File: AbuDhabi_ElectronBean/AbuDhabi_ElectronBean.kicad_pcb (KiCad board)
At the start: 2 copper layers, 174.2 x 163.6 mm, 18 parts, among them J12 Sensor, J13 Bomba, J14 Eingang - obere Pins, J15 Eingang - obere Pins, J16 Power, J17 Control, J18 Data, J19 Ext. versorgung conn, J20 MUX_output, U1 74HC139P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

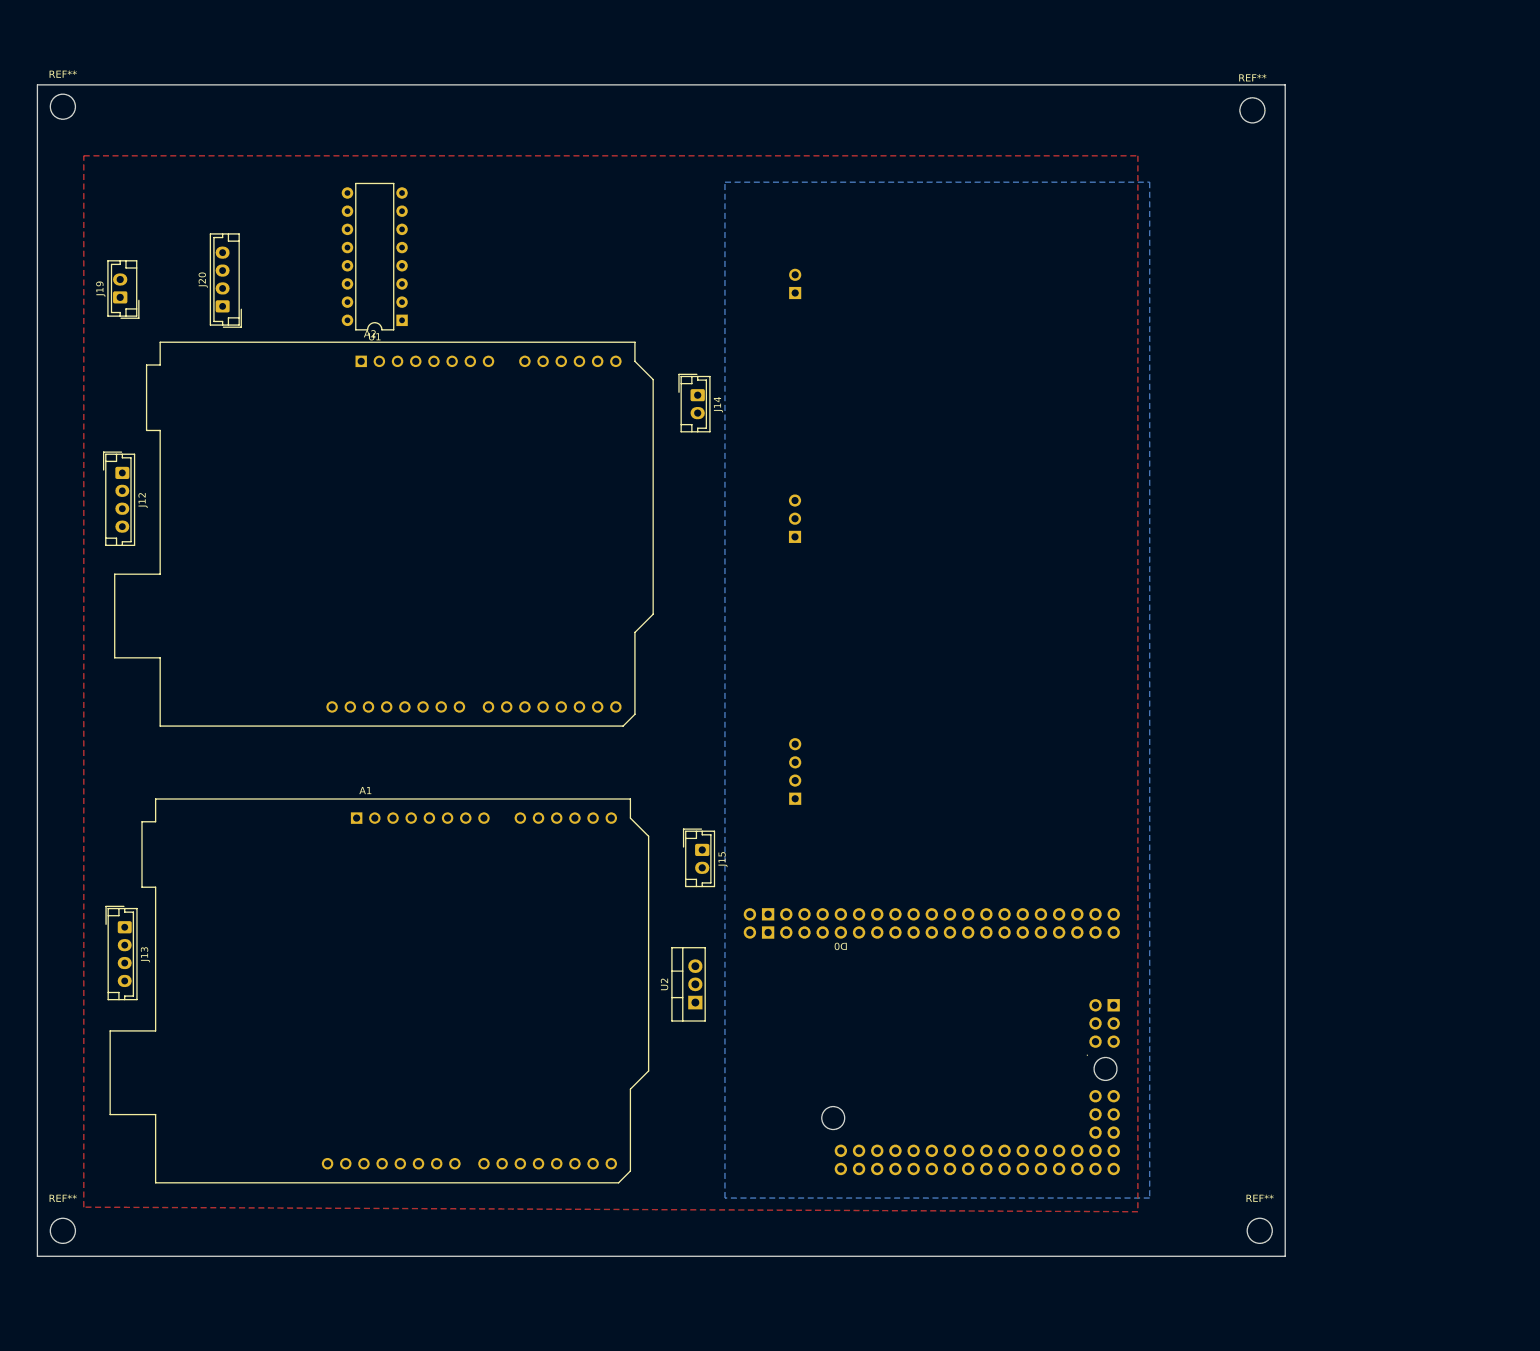
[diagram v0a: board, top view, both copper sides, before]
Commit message: Arduino Mega footpring change and LEDs addition
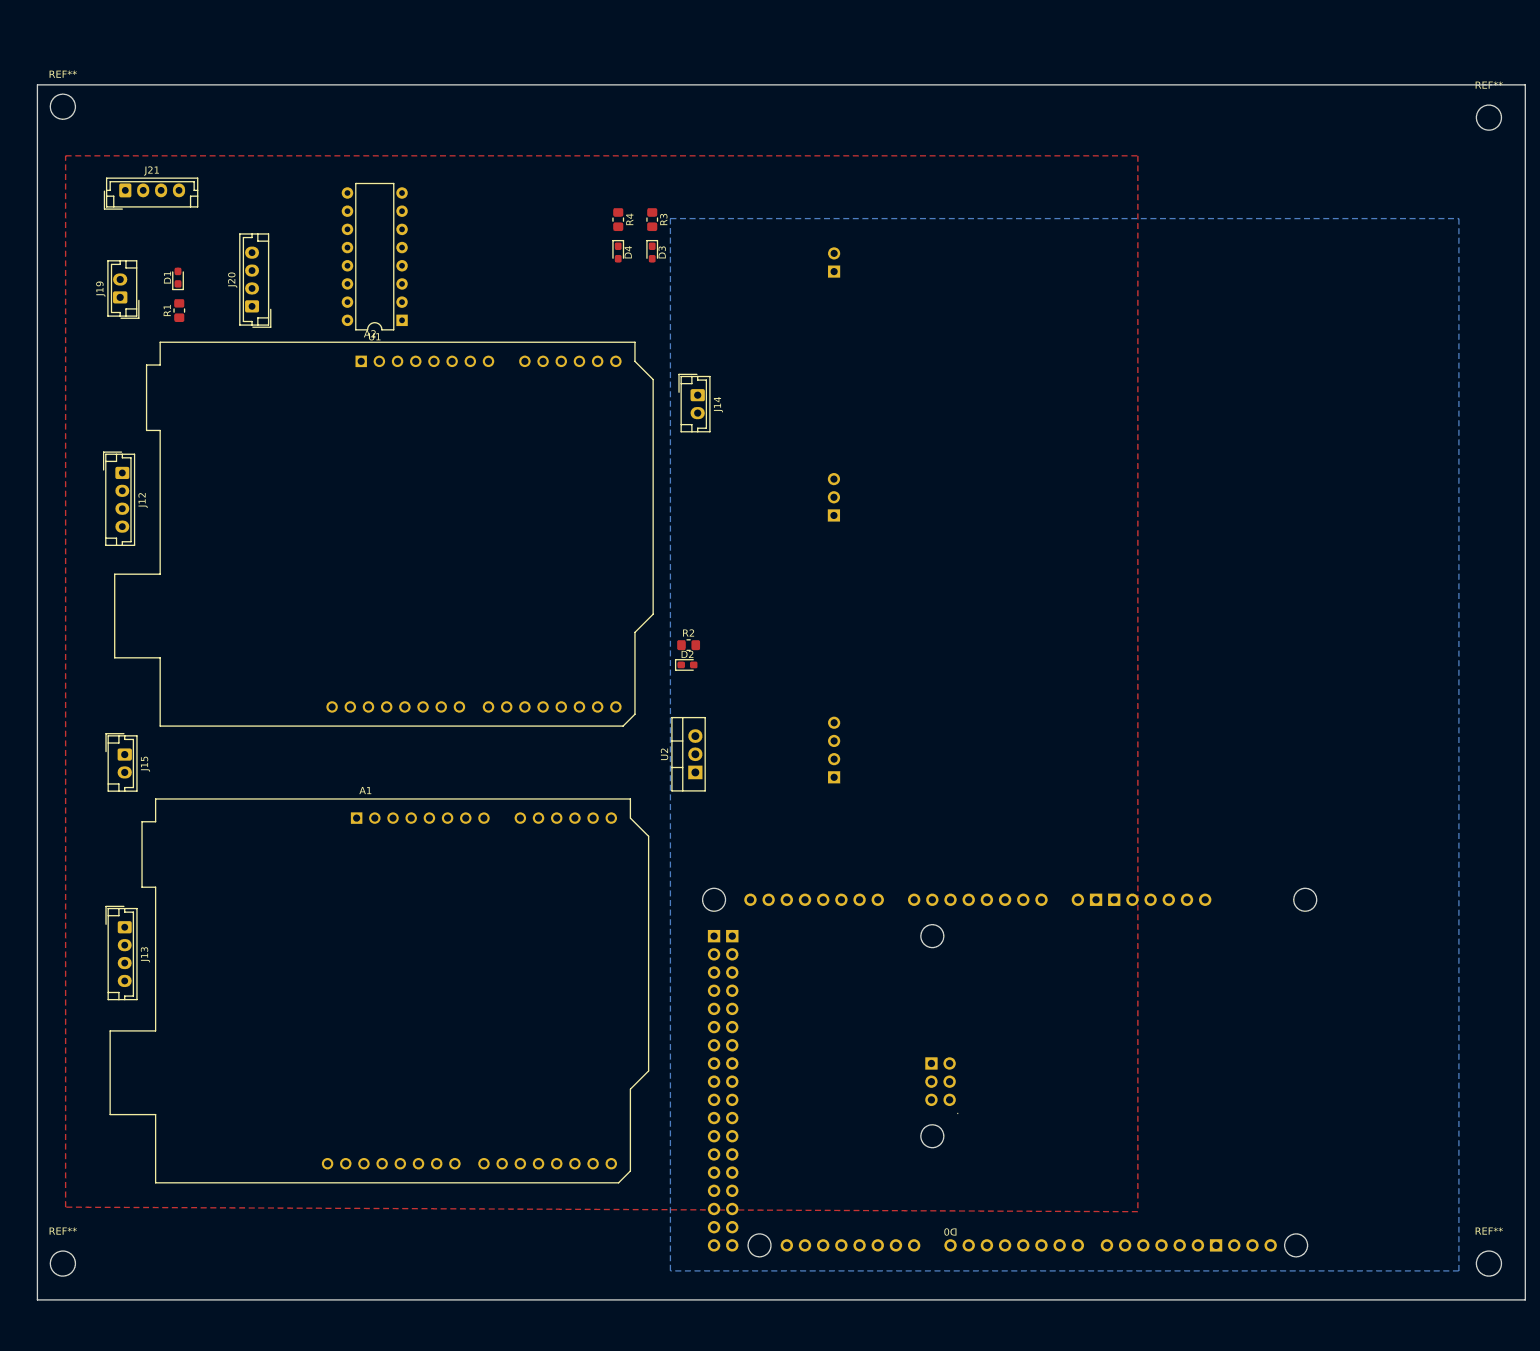
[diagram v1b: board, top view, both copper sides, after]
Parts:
- added D1: LED, LED_SMD:LED_0603_1608Metric_Pad1.05x0.95mm_HandSolder, F.Cu at (40.5, 47.7)
- added D2: LED, LED_SMD:LED_0603_1608Metric_Pad1.05x0.95mm_HandSolder, F.Cu at (111.6, 101.8)
- added D3: LED, LED_SMD:LED_0603_1608Metric_Pad1.05x0.95mm_HandSolder, F.Cu at (106.7, 44.2)
- added D4: LED, LED_SMD:LED_0603_1608Metric_Pad1.05x0.95mm_HandSolder, F.Cu at (101.9, 44.2)
- added J21: Versorgung(opt), Connector_JST:JST_EH_B4B-EH-A_1x04_P2.50mm_Vertical, F.Cu at (33.1, 35.6)
- added R1: 220, Resistor_SMD:R_0805_2012Metric_Pad1.20x1.40mm_HandSolder, F.Cu at (40.6, 52.3)
- added R2: 220, Resistor_SMD:R_0805_2012Metric_Pad1.20x1.40mm_HandSolder, F.Cu at (111.8, 99.1)
- added R3: 220, Resistor_SMD:R_0805_2012Metric_Pad1.20x1.40mm_HandSolder, F.Cu at (106.7, 39.6)
- added R4: 220, Resistor_SMD:R_0805_2012Metric_Pad1.20x1.40mm_HandSolder, F.Cu at (101.9, 39.6)
- A3: footprint Arduino:Footprint_Mega2560_Pro_Socket -> Arduino:Arduino_Mega2560_R3_Shield; moved to F.Cu
- moved A3 102.2 mm to (211.8, 132.1), turned to 180 degrees
- moved J15 81.7 mm to (33.0, 114.3)
- moved REF** 33.0 mm to (223.5, 25.4)
- moved REF** 32.3 mm to (223.5, 185.4)
- moved U2 32.1 mm to (112.7, 116.8)
- moved J16 6.20 mm to (132.1, 46.9)
- moved J17 6.20 mm to (132.1, 81.0)
- moved J18 6.20 mm to (132.1, 117.5)
- moved REF** 4.57 mm to (24.4, 185.4)
- moved J20 4.11 mm to (50.8, 51.8)
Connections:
- A2 pad 15: /Rx1 -> /Rx3
- A2 pad 16: /Tx1 -> /Tx3
- A3 pad D5: unconnected-(A3-PadD5) -> /IO5
- J12 pad 1: /GND ext -> GND
- J13 pad 1: /GND ext -> GND
- J16 pad 1: /GND Ard -> GND
- J16 pad 2: /5V -> /5VExt
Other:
- board size 174.2 x 163.6 mm -> 207.8 x 169.7 mm

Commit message: A bit of order
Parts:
- moved J20 2.54 mm to (53.3, 51.8)
- moved R1 2.30 mm to (41.6, 50.2)
- moved D1 2.30 mm to (41.4, 45.6)
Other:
- board text added: "24V ext. source"
- board text added: "5V first output"
- board text added: "Ard. output"
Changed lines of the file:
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@@
   )
   (footprint "LED_SMD:LED_0603_1608Metric_Pad1.05x0.95mm_HandSolder" (layer "F.Cu")
-    (at 40.46 47.745 90)
+    (at 41.375 45.63 90)
     (descr "LED SMD 0603 (1608 Metric), square (rectangular) end terminal, IPC_7351 nominal, (Body size source: http://www.tortai-tech.com/upload/download/2011102023233369053.pdf), generated with kicad-footprint-generator")
     (tags "LED handsolder")
@@
   )
   (footprint "Connector_JST:JST_EH_B4B-EH-A_1x04_P2.50mm_Vertical" (layer "F.Cu")
-    (at 50.8 51.756 90)
+    (at 53.34 51.756 90)
     (descr "JST EH series connector, B4B-EH-A (http://www.jst-mfg.com/product/pdf/eng/eEH.pdf), generated with kicad-footprint-generator")
     (tags "connector JST EH vertical")
@@
     (fp_arc (start 98.552 0.254) (mid 96.52 0.914237) (end 94.488 0.254)
       (stroke (width 0.15) (type solid)) (layer "B.CrtYd"))
-    (fp_arc (start 99.8728 -1.7018) (mid 99.650929 -1.077971) (end 99.314 -0.508)
+    (fp_arc (start 99.8728 -1.7018) (mid 99.650928 -1.077972) (end 99.314 -0.508)
       (stroke (width 0.15) (type solid)) (layer "B.CrtYd"))
     (fp_circle (center 13.97 -2.54) (end 17.42 -2.54)
@@
   )
   (footprint "Resistor_SMD:R_0805_2012Metric_Pad1.20x1.40mm_HandSolder" (layer "F.Cu")
-    (at 40.64 52.34 90)
+    (at 41.555 50.225 90)
     (descr "Resistor SMD 0805 (2012 Metric), square (rectangular) end terminal, IPC_7351 nominal with elongated pad for handsoldering. (Body size source: IPC-SM-782 page 72, https://www.pcb-3d.com/wordpress/wp-content/uploads/ipc-sm-782a_amendment_1_and_2.pdf), generated with kicad-footprint-generator")
     (tags "resistor handsolder")
@@
   (gr_line (start 190.856 127.565) (end 190.856 25.457)
     (stroke (width 0.2) (type solid)) (layer "B.SilkS"))
+  (gr_rect (start 99.06 35.56) (end 109.22 48.26)
+    (stroke (width 0.15) (type default)) (fill none) (layer "F.SilkS"))
+  (gr_rect (start 109.22 96.52) (end 114.3 104.14)
+    (stroke (width 0.15) (type default)) (fill none) (layer "F.SilkS"))
+  (gr_rect (start 39.015 43.605) (end 44.095 53.765)
+    (stroke (width 0.15) (type default)) (fill none) (layer "F.SilkS"))
   (gr_line (start 228.6 190.5) (end 228.6 20.828)
     (stroke (width 0.1) (type solid)) (layer "Edge.Cuts"))
@@
   (gr_line (start 228.6 20.828) (end 20.828 20.828)
     (stroke (width 0.1) (type solid)) (layer "Edge.Cuts"))
+  (gr_text "Ard. output" (at 111.76 48.26 90) (layer "F.SilkS")
+    (effects (font (size 1 1) (thickness 0.15)) (justify left bottom))
+  )
+  (gr_text "24V ext. source" (at 116.84 104.14 90) (layer "F.SilkS")
+    (effects (font (size 1 1) (thickness 0.15)) (justify left bottom))
+  )
+  (gr_text "5V first output" (at 46.635 53.765 90) (layer "F.SilkS")
+    (effects (font (size 1 1) (thickness 0.15)) (justify left bottom))
+  )
   (dimension (type aligned) (layer "F.Cu")
     (pts (xy 132.69 75.368) (xy 132.69 47.428))

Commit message: Nothing
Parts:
- renumbered REF** to Hole1, REF** to Hole2, REF** to Hole3, REF** to Hole4
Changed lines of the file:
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@@
     (tags "mounting hole 3.5mm no annular")
     (attr exclude_from_pos_files exclude_from_bom)
-    (fp_text reference "REF**" (at 0 -4.5) (layer "F.SilkS")
+    (fp_text reference "Hole2" (at 0 -4.5) (layer "F.SilkS")
         (effects (font (size 1 1) (thickness 0.15)))
     )
@@
     (tags "mounting hole 3.5mm no annular")
     (attr exclude_from_pos_files exclude_from_bom)
-    (fp_text reference "REF**" (at 0 -4.5) (layer "F.SilkS")
+    (fp_text reference "Hole1" (at 0 -4.5) (layer "F.SilkS")
         (effects (font (size 1 1) (thickness 0.15)))
     )
@@
     (fp_arc (start 98.552 0.254) (mid 96.52 0.914237) (end 94.488 0.254)
       (stroke (width 0.15) (type solid)) (layer "B.CrtYd"))
-    (fp_arc (start 99.8728 -1.7018) (mid 99.650928 -1.077972) (end 99.314 -0.508)
+    (fp_arc (start 99.8728 -1.7018) (mid 99.650934 -1.077968) (end 99.314 -0.508)
       (stroke (width 0.15) (type solid)) (layer "B.CrtYd"))
     (fp_circle (center 13.97 -2.54) (end 17.42 -2.54)
@@
     (tags "mounting hole 3.5mm no annular")
     (attr exclude_from_pos_files exclude_from_bom)
-    (fp_text reference "REF**" (at 0 -4.5) (layer "F.SilkS")
+    (fp_text reference "Hole4" (at 0 -4.5) (layer "F.SilkS")
         (effects (font (size 1 1) (thickness 0.15)))
     )
@@
     (tags "mounting hole 3.5mm no annular")
     (attr exclude_from_pos_files exclude_from_bom)
-    (fp_text reference "REF**" (at 0 -4.5) (layer "F.SilkS")
-        (effects (font (size 1 1) (thickness 0.15)))
-    )
+    (fp_text reference "Hole3" (at 0 -4.5) (layer "F.SilkS")
+        (effects (font (size 1 1) (thickness 0.15)))
+    )

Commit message: Routing part 1
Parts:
- moved D3 32.4 mm to (75.9, 34.1), turned to 90 degrees
- moved R3 30.8 mm to (75.9, 38.7)
- moved U1 28.0 mm to (60.3, 28.2), turned to 0 degrees
- moved D4 23.6 mm to (80.6, 34.1), turned to 90 degrees
- moved R4 21.3 mm to (80.6, 38.7)
- moved J20 16.0 mm to (52.7, 35.8), turned to -90 degrees
- moved A3 8.02 mm to (208.7, 124.7)
- moved Hole3 8.02 mm to (220.3, 18.0)
- moved J16 8.02 mm to (128.9, 39.5)
- moved J17 8.02 mm to (128.9, 73.6)
- moved J18 8.02 mm to (128.9, 110.2)
- moved R2 8.02 mm to (108.6, 91.7)
- moved J21 8.02 mm to (29.9, 28.2)
- moved A1 8.02 mm to (62.2, 115.8)
- moved A2 8.02 mm to (62.9, 52.1)
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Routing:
- net /MUX_1sel: track 0.00 -> 296.6 mm, vias 0 -> 1
- net /MUX_2sel: track 0.00 -> 282.3 mm, vias 0 -> 2
- net /MUX_ena: track 0.00 -> 274.2 mm
- net /5VExt: track 0.00 -> 251.5 mm, vias 0 -> 4
- net +3.3V: track 0.00 -> 205.7 mm
- net +24V: track 0.00 -> 197.2 mm
- net /5Vard: track 0.00 -> 191.4 mm, vias 0 -> 1
- net /SCL: track 0.00 -> 178.3 mm, vias 0 -> 2
- net /IO4: track 0.00 -> 149.4 mm, vias 0 -> 2
- net /IO5: track 0.00 -> 148.1 mm, vias 0 -> 1
- net /SDA: track 0.00 -> 143.1 mm, vias 0 -> 1
- net /IO3: track 0.00 -> 126.0 mm, vias 0 -> 1
- net /Tx3: track 0.00 -> 125.6 mm, vias 0 -> 1
- net /EN485: track 0.00 -> 123.1 mm, vias 0 -> 1
- net /Rx3: track 0.00 -> 116.9 mm, vias 0 -> 1
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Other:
- board size 207.8 x 169.7 mm -> 207.8 x 182.1 mm

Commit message: Everything routed and DRC checked and corrected, ready to print
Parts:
- moved U2 25.7 mm to (109.5, 83.8)
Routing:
- net /MUX_2sel: track 282.3 -> 285.1 mm, vias 2 -> 1
- net /RxS: track 87.8 -> 85.9 mm
- net /5VExt: track 251.5 -> 253.2 mm
- net /MUX_ena: track 274.2 -> 272.6 mm, vias 0 -> 2
- net +24V: track 197.2 -> 198.1 mm
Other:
- board text added: "24V ext. <- source"
- board text added: "Arduino Mega 2560"
- board text added: "Ext. source input ->"
- board text added: "LCS screen"
- board text added: "MUX"
- board text added: "MUX output"
- board text added: "Pump"
- board text added: "RS232 comms"
- board text added: "RS232 shield"
- board text added: "RS485 comms"
- board text added: "RS485 shield"
- board text added: "Sensor"
- board text added: "TSRN1-2450"
- board text added: "opt. power output"
- board text removed: "24V ext. source"
